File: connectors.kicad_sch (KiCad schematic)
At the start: 4 parts, among them J1 Conn_01x04_Pin, J2 Conn_01x04_Pin, J3 Conn_01x09_Pin, J4 Conn_02x03_Odd_Even

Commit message: Assigned Footprints.
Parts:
- J1, J2: footprint (none) -> Connector_PinHeader_2.54mm:PinHeader_1x04_P2.54mm_Vertical
- J3: footprint (none) -> Connector_PinHeader_2.54mm:PinHeader_1x09_P2.54mm_Vertical
- J4: footprint (none) -> Connector_PinHeader_2.54mm:PinHeader_2x03_P2.54mm_Vertical
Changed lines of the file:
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@@
 			)
 		)
-		(property "Footprint" ""
+		(property "Footprint" "Connector_PinHeader_2.54mm:PinHeader_1x04_P2.54mm_Vertical"
 			(at 113.03 107.95 0)
 			(effects
@@
 			)
 		)
-		(property "Footprint" ""
+		(property "Footprint" "Connector_PinHeader_2.54mm:PinHeader_1x04_P2.54mm_Vertical"
 			(at 139.7 101.6 0)
 			(effects
@@
 			)
 		)
-		(property "Footprint" ""
+		(property "Footprint" "Connector_PinHeader_2.54mm:PinHeader_1x09_P2.54mm_Vertical"
 			(at 113.03 137.16 0)
 			(effects
@@
 			)
 		)
-		(property "Footprint" ""
+		(property "Footprint" "Connector_PinHeader_2.54mm:PinHeader_2x03_P2.54mm_Vertical"
 			(at 140.97 129.54 0)
 			(effects

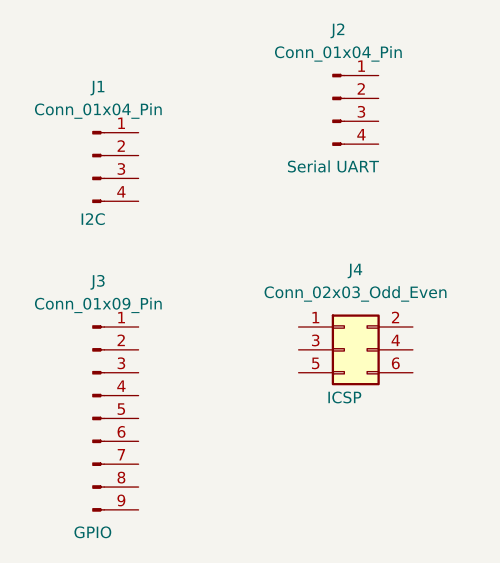
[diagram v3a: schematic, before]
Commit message: Completed Wiring in second sheet.
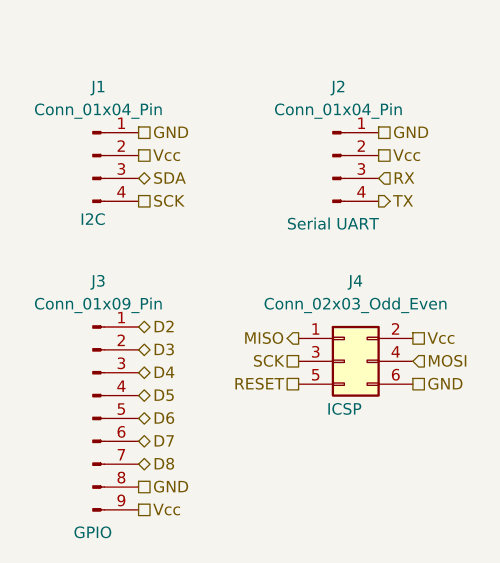
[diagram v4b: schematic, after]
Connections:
- net GND: now reaches J1.1 (Pin_1)
- net GND: now also J2.1 (Pin_1), J3.8 (Pin_8), J4.6 (Pin_6)
- net Vcc: now reaches J1.2 (Pin_2)
- net Vcc: now also J2.2 (Pin_2), J3.9 (Pin_9), J4.2 (Pin_2)
- net SDA: now reaches J1.3 (Pin_3)
- net SCK: now reaches J1.4 (Pin_4)
- net SCK: now also J4.3 (Pin_3)
- net RX: now reaches J2.3 (Pin_3)
- net TX: now reaches J2.4 (Pin_4)
- net D2: now reaches J3.1 (Pin_1)
- net D3: now reaches J3.2 (Pin_2)
- net D4: now reaches J3.3 (Pin_3)
- net D5: now reaches J3.4 (Pin_4)
- net D6: now reaches J3.5 (Pin_5)
- net D7: now reaches J3.6 (Pin_6)
- net D8: now reaches J3.7 (Pin_7)
- net MISO: now reaches J4.1 (Pin_1)
- net MOSI: now reaches J4.4 (Pin_4)
- net RESET: now reaches J4.5 (Pin_5)
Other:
- moved on the sheet: J2, J4
